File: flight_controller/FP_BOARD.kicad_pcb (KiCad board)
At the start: 6 copper layers, 100 x 100 mm, 251 parts, among them J1 HX PZ2.54-3X4P ZZ, J10 CNJMA2012WV-S-10P, J11 A1257WV-S-6P-LCP, J12 A1257WV-S-6P-LCP, J13 A1257WV-S-6P-LCP, J14 HR911105A_C12074, J15 A1257WV-S-6P-LCP, J16 HCZZ0494-2, J17 HCZZ0494-4, J18 A1251WV-S-4P, J19 A1251WV-S-6P, J2 B3B-ZR-SM4-TF(LF)(SN), J20 A1251WV-S-3P, J21 HB-PH9-12727PB2GOB, J22 HB-PH9-12727PB2GOB, J3 HX PZ2.54-3X4P ZZ, J4 HX PZ2.54-3X4P ZZ, J5 SM04B-SRSS-TB(LF)(SN), J6 A1257WV-S-6P-LCP, J7 HCZZ0494-4, J8 HCZZ0494-4, J9 A1257WV-S-6P-LCP, Q1 AO3400A, SW1 6.0*6.0*6.0, SW2 6.0*6.0*6.0, U10 24LC64-I/SN, U11 FM25V02A-GTR, U12 MPU6500, U13 MS561101BA03-50, U14 LAN8742AI-CZ, U15 SN74LVC1G07DBVR_C19829659, U2 STM32H743IIT6, U4 STM32F103C8T6, U5 SN74LVC2G240DCTR, U56 ICM-20689, U7 TJA1051T/3/1J, U8 TJA1051T/3/1J, U9 W25Q512JVFIQ, X1 XKXEL89CLI-SUAYLC-32.768K, X2 XL2EL89CLI-111YLC-16M, X3 X322524MLB4SI_C5210646, X4 XL2EL89CMI-111YLC-25M

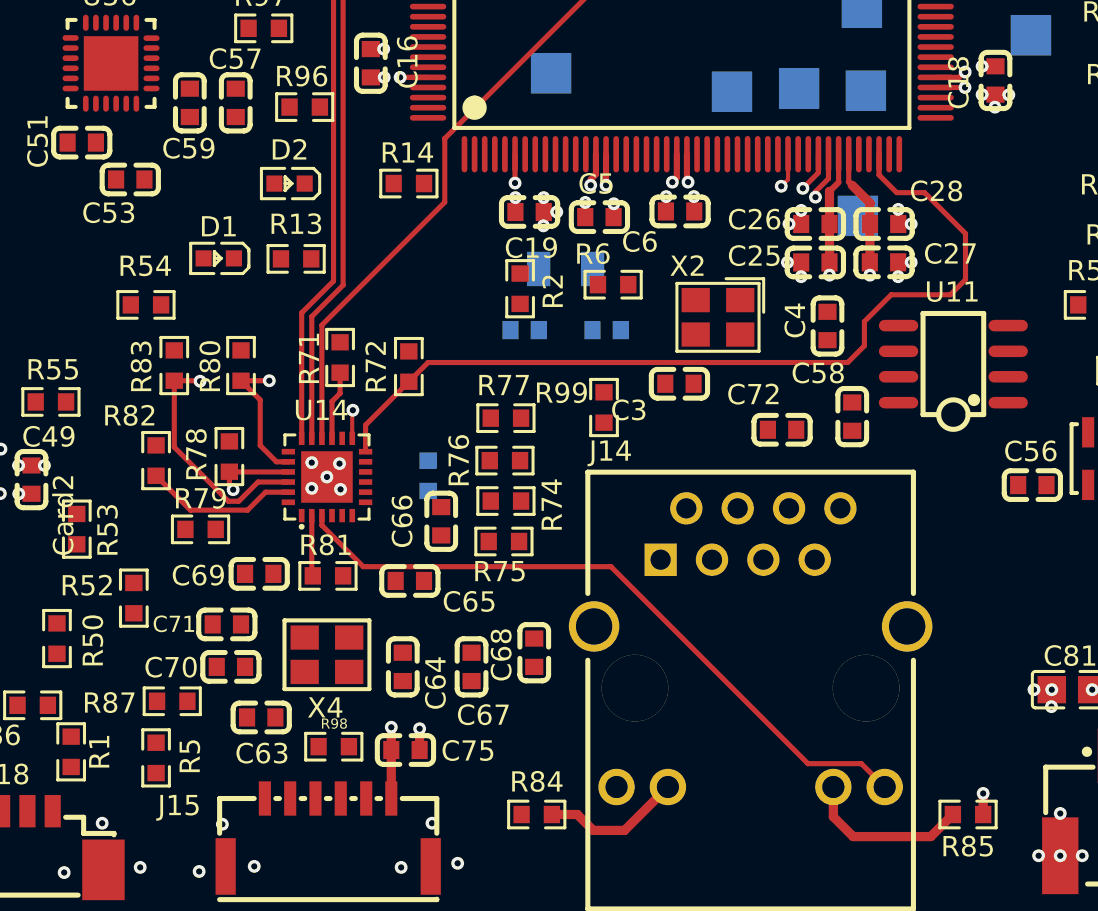
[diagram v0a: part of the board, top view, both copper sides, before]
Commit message: Trying to route ethernet
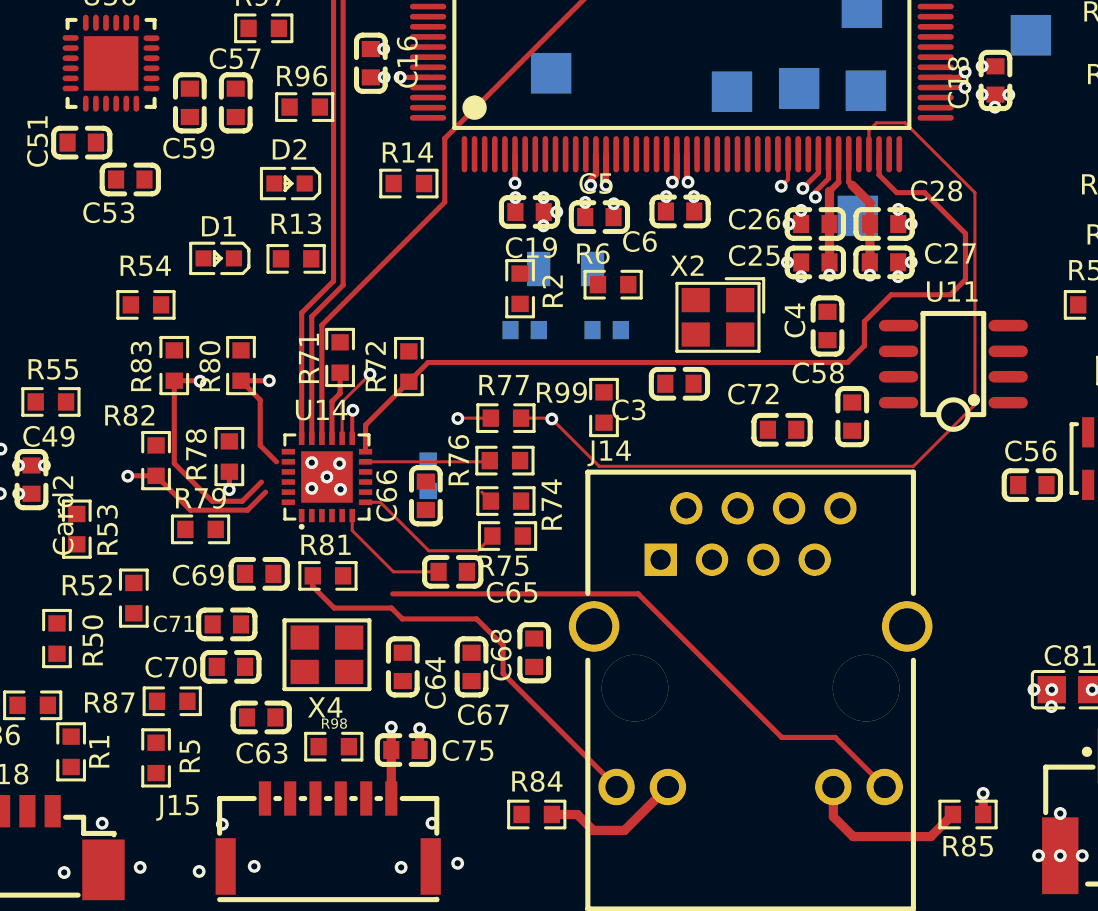
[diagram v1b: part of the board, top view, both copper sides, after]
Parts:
- moved C65 2.17 mm to (124.3, 116.2)
- moved C66 1.47 mm to (122.9, 112.5)
- moved R75 0.32 mm to (127.0, 114.5)
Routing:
- net /ETH_REF_CLK: track 0.00 -> 43.2 mm, vias 0 -> 1
- net /ETH/ETH_TXN: track 6.72 -> 40.2 mm
- net /ETH/ETH_RXP: track 7.61 -> 39.8 mm, vias 0 -> 1
- net /ETH/ETH_RXN: track 11.7 -> 42.6 mm
- net /ETH/ETH_TXP: track 3.88 -> 23.7 mm
- net /ETH/ETH_LED2: track 3.00 -> 20.5 mm
- net Net-(U14-~{INT}/REFCLKO): track 0.00 -> 13.8 mm, vias 0 -> 2
- net Net-(U14-RXD1/MODE1): track 0.00 -> 7.57 mm
- net Net-(U14-CRS_DV/MODE2): track 0.00 -> 6.16 mm
- net Net-(U14-VDDCR): track 0.00 -> 5.85 mm
- net /ETH/ETH_LED1: track 33.7 -> 28.3 mm
- net Net-(U14-RXD0/MODE0): track 0.00 -> 0.62 mm

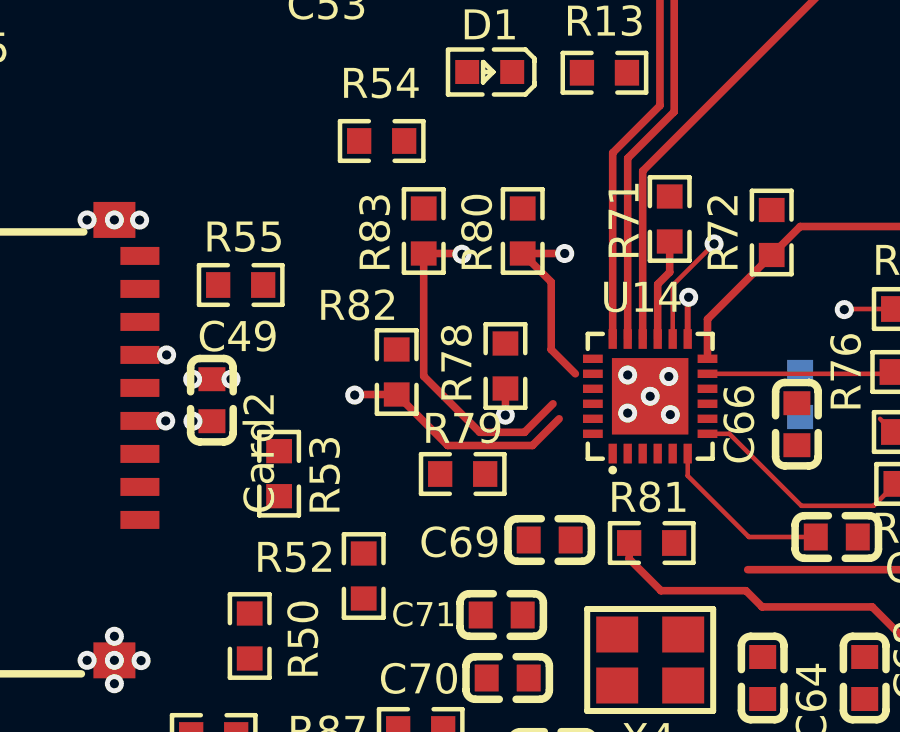
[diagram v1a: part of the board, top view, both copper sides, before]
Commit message: Changed eth net name and started diff route , added custom rules file for diff
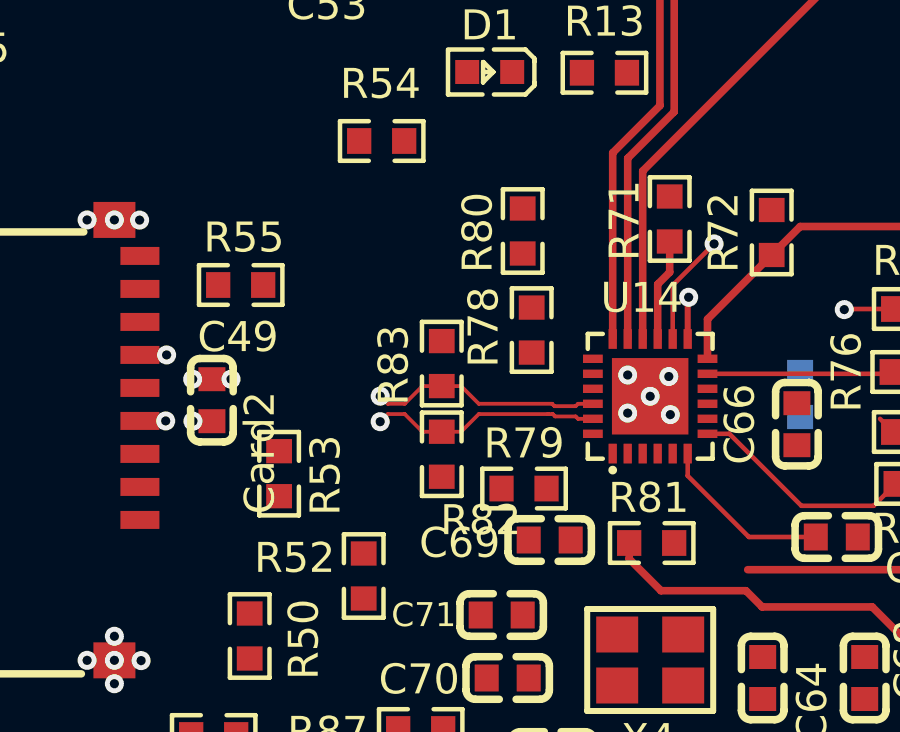
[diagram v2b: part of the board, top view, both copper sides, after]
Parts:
- moved R83 4.46 mm to (111.1, 110.5)
- moved R82 3.13 mm to (111.1, 113.5), turned to -90 degrees
- moved R79 2.10 mm to (113.8, 114.6)
- moved R78 1.48 mm to (114.1, 109.4)
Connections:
- net /ETH/ETH_RXN renamed /ETH/ETH_RX_N
- net /ETH/ETH_RXP renamed /ETH/ETH_RX_P
- net /ETH/ETH_TXN renamed /ETH/ETH_TX_N
- net /ETH/ETH_TXP renamed /ETH/ETH_TX_P
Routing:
- net /ETH/ETH_TX_N: track 40.2 -> 0.00 mm, vias 1 -> 0
- net /ETH/ETH_TX_P: track 23.7 -> 0.00 mm, vias 1 -> 0
- net /ETH/ETH_RX_P: track 39.8 -> 44.8 mm
- net /ETH/ETH_RX_N: track 42.6 -> 45.7 mm

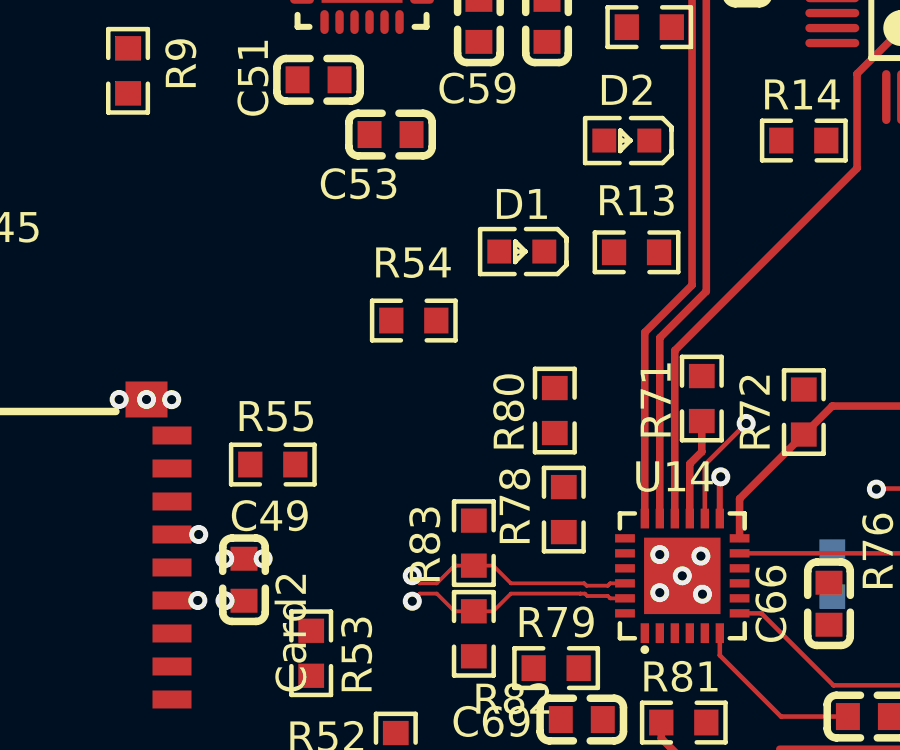
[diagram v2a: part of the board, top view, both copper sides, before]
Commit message: Added some eth lines
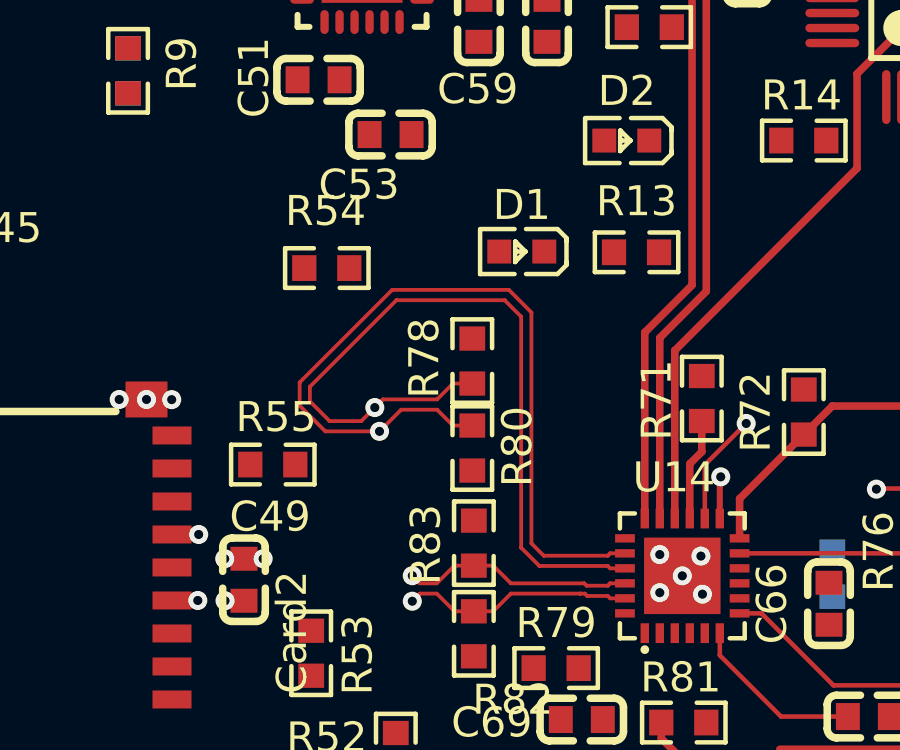
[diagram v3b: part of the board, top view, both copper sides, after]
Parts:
- moved R78 5.82 mm to (111.0, 104.4)
- moved R54 3.39 mm to (106.2, 101.3)
- moved R80 3.02 mm to (111.0, 107.3), turned to -90 degrees
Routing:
- net /ETH/ETH_TX_N: track 0.00 -> 69.6 mm, vias 0 -> 1
- net /ETH/ETH_TX_P: track 0.00 -> 67.4 mm, vias 0 -> 1
- net /ETH/ETH_RX_N: track 45.7 -> 47.8 mm

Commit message: Added stuff
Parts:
- removed C68: CL10B103KB8NNNC (10nf , 0603 , 50v , X7R), easyeda2kicad:C0603
- removed C71: CL10A106MA8NRNC (10uf , 0603 ,25v ,X5R), easyeda2kicad:C0603
- moved C70 11.9 mm to (114.3, 109.1), turned to -90 degrees
- moved R81 11.3 mm to (127.5, 122.8), turned to 90 degrees
- moved C69 1.61 mm to (115.0, 114.8), turned to 90 degrees
- moved C63 1.47 mm to (116.2, 123.2)
- moved R79 1.05 mm to (113.0, 114.0), turned to -90 degrees
- moved C66 0.89 mm to (122.7, 111.6), turned to -90 degrees
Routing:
- net Net-(U14-XTAL2): track 0.00 -> 10.5 mm
- net /ETH/ETH_LED1: track 28.3 -> 37.7 mm, vias 0 -> 2
- net Net-(U14-XTAL1/CLKIN): track 0.00 -> 9.14 mm
- net 3V3: track 89.1 -> 97.3 mm, vias 67 -> 76
- net Net-(U14-RXD0/MODE0): track 0.62 -> 8.14 mm
- net Net-(U14-RXER/PHYAD0): track 0.00 -> 3.51 mm, vias 0 -> 1
- net Net-(U14-RBIAS): track 0.00 -> 3.36 mm
- net /ETH/ETH_LED2: track 20.5 -> 23.4 mm, vias 0 -> 2
- net 5V: track 23.7 -> 21.2 mm, vias 28 -> 29
- net GND: track 144.4 -> 146.6 mm, vias 271 -> 278
- net Net-(U14-CRS_DV/MODE2): track 6.16 -> 7.40 mm

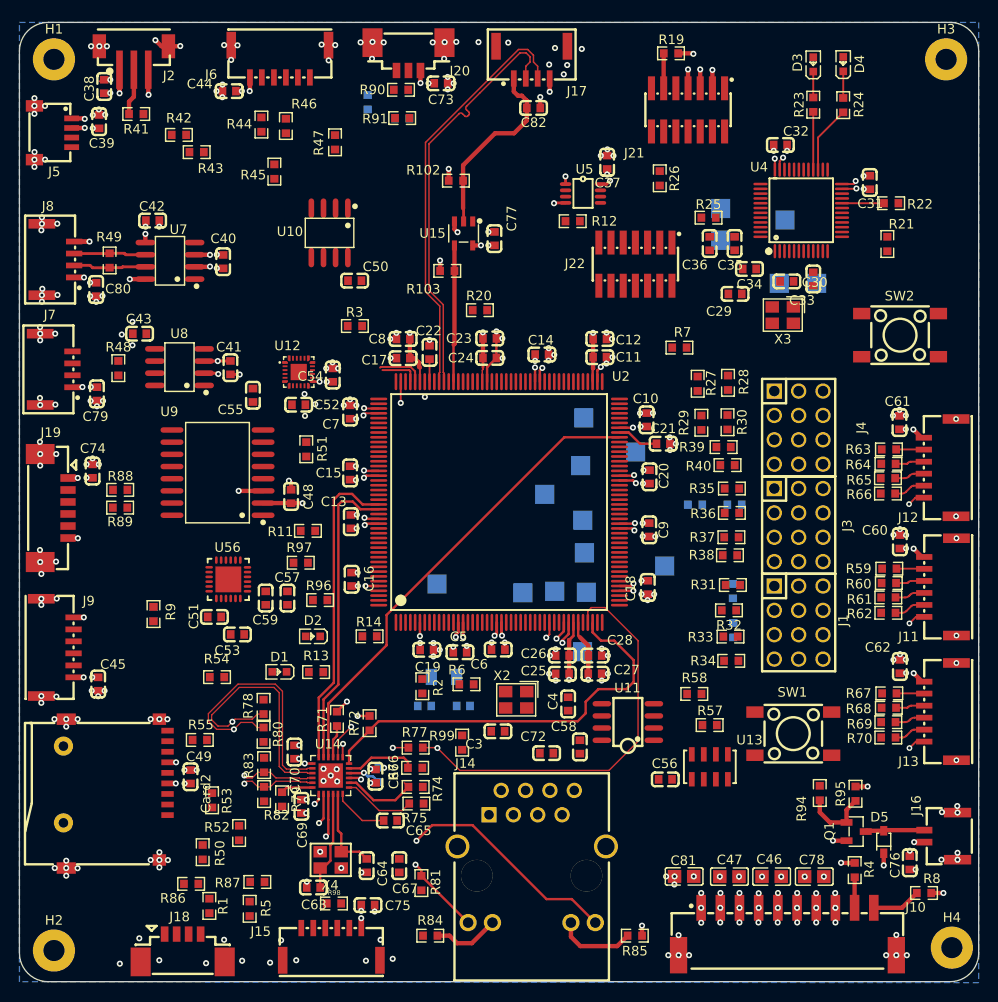
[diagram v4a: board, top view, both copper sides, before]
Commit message: Routed all match length buses
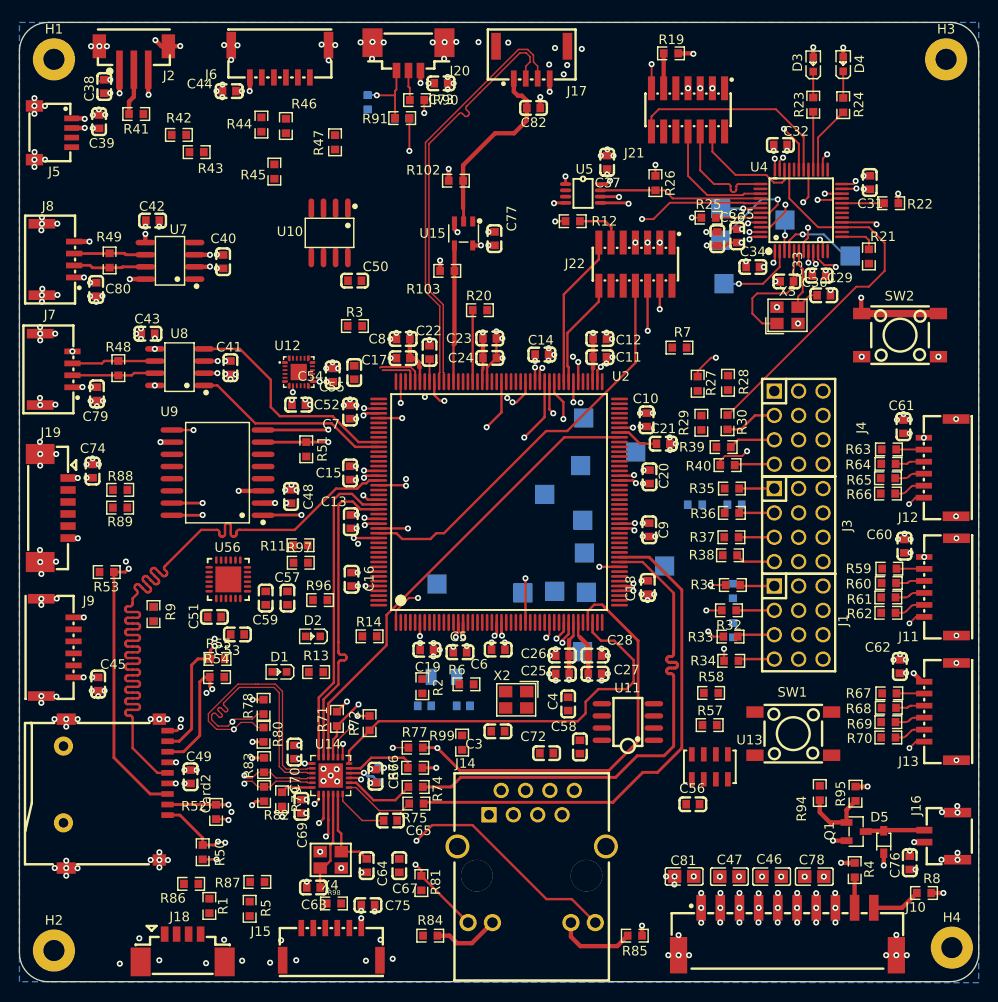
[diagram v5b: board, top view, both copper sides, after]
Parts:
- moved R53 26.2 mm to (94.7, 90.3), turned to 180 degrees
- moved C55 10.8 mm to (120.5, 69.5)
- moved C29 9.25 mm to (169.4, 61.5), turned to 180 degrees
- moved R55 8.65 mm to (106.2, 99.4)
- moved TP13 5.75 mm to (159.1, 60.3)
- moved TP15 4.51 mm to (172.2, 57.4)
- moved C56 3.87 mm to (155.8, 114.5)
- moved R52 3.26 mm to (106.1, 115.3)
- moved R21 2.32 mm to (174.2, 57.5)
- moved R90 1.99 mm to (127.0, 41.1), turned to 180 degrees
- moved R58 1.75 mm to (157.7, 103.0)
- moved R11 1.69 mm to (114.9, 87.5)
- moved C36 0.94 mm to (158.3, 55.6), turned to -90 degrees
- moved C43 0.88 mm to (99.0, 65.5)
- moved C35 0.85 mm to (160.4, 55.3), turned to -90 degrees
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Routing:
- net /SDMMC2_CLK: track 0.00 -> 86.3 mm
- net /SDMMC2_D0: track 0.00 -> 84.0 mm, vias 0 -> 2
- net /SDMMC2_CMD: track 0.00 -> 83.8 mm, vias 0 -> 2
- net /SDMMC2_D1: track 0.00 -> 83.7 mm, vias 0 -> 2
- net /SD_CARD_DETECT: track 0.00 -> 83.7 mm, vias 0 -> 2
- net /SDMMC2_D3: track 0.00 -> 83.5 mm, vias 0 -> 2
- net /SDMMC2_D2: track 0.00 -> 83.5 mm, vias 0 -> 2
- net /ETH_RXD1: track 0.00 -> 53.7 mm
- net /ETH_RXD0: track 0.00 -> 53.6 mm
- net /ETH_NRST: track 3.42 -> 56.6 mm, vias 0 -> 2
- net /IO_CH1: track 0.00 -> 50.1 mm, vias 0 -> 2
- net /IO_CH4: track 0.00 -> 49.4 mm, vias 0 -> 2
- net /IO_CH2: track 0.00 -> 49.4 mm, vias 0 -> 2
- net /QUADSPI_BK1_IO0: track 0.00 -> 48.7 mm, vias 0 -> 2
- net /QUADSPI_CLK: track 0.00 -> 48.7 mm, vias 0 -> 2
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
